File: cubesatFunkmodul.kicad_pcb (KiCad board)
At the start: 2 copper layers, 14 parts, among them IC1 74HC4050, U2 ATMEGA128-16AU, Y1 Crystal_GND23

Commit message: Cleares PCB
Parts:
- removed C1, C2, C3: C, Capacitors_SMD:C_0603
- removed C4, C5: 10pF, Capacitors_SMD:C_0603_HandSoldering
- removed C6: C, Capacitors_SMD:C_0603_HandSoldering
- removed D1: D, Diodes_SMD:D_0603
- removed IC1: 74HC4050, Housings_SSOP:SSOP-16_5.3x6.2mm_Pitch0.65mm
- removed L1: Ferrite_Bead, Inductors_SMD:L_0603_HandSoldering
- removed R1, R2, R3: R, Resistors_SMD:R_0603_HandSoldering
- removed U2: ATMEGA128-16AU, Housings_QFP:TQFP-64_14x14mm_Pitch0.8mm
- removed Y1: Crystal_GND23, Crystals:Crystal_SMD_0603-4pin_6.0x3.5mm_HandSoldering

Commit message: Adds new submodules
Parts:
- added C1: 10pF, Capacitors_SMD:C_0603_HandSoldering, F.Cu at (113.8, 115.8)
- added C2: 10pF, Capacitors_SMD:C_0603_HandSoldering, F.Cu at (121.6, 118.4)
- added C3: C, Capacitors_SMD:C_0603_HandSoldering, F.Cu at (140.7, 97.3)
- added C4: 100nF, Capacitors_SMD:C_0603, F.Cu at (136.9, 112.3)
- added C5: 100nF, Capacitors_SMD:C_0603, F.Cu at (157.0, 102.4)
- added C6: 100nF, Capacitors_SMD:C_0603, F.Cu at (153.2, 97.8)
- added D1: D, Diodes_SMD:D_0603, F.Cu at (155.3, 113.3)
- added IC1: 74HC4050, Housings_SSOP:SSOP-16_5.3x6.2mm_Pitch0.65mm, F.Cu at (102.5, 109.7)
- added L1: 10nH, Inductors_SMD:L_0603_HandSoldering, F.Cu at (157.6, 106.9)
- added R1: R, Resistors_SMD:R_0603_HandSoldering, F.Cu at (141.8, 104.6)
- added R2: R, Resistors_SMD:R_0603_HandSoldering, F.Cu at (147.2, 113.0)
- added R3: R, Resistors_SMD:R_0603_HandSoldering, F.Cu at (148.5, 103.1)
- added U1: ATMEGA128-16AU, Housings_QFP:TQFP-64_14x14mm_Pitch0.8mm, F.Cu at (123.2, 99.1)
- added Y1: Crystal_GND23, Crystals:Crystal_SMD_EuroQuartz_X22-4pin_2.5x2.0mm_HandSoldering, F.Cu at (130.7, 117.7)
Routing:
- net /Funkmodul1/+3.3V: track 0.00 -> 20.1 mm, vias 0 -> 1

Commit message: Adds Connectors
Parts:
- removed IC1: 74HC4050, Housings_SSOP:SSOP-16_5.3x6.2mm_Pitch0.65mm
- added C10: 100nF, Capacitors_SMD:C_0603_HandSoldering, F.Cu at (68.6, 101.1)
- added C11: 100nF, Capacitors_SMD:C_0603_HandSoldering, F.Cu at (88.7, 107.8)
- added C12: 100nF, Capacitors_SMD:C_0603_HandSoldering, F.Cu at (88.7, 100.1)
- added C13: 47µF, Capacitors_SMD:C_1210_HandSoldering, F.Cu at (235.5, 73.2)
- added C14: 47µF, Capacitors_SMD:C_1210_HandSoldering, F.Cu at (254.6, 99.6)
- added C15: 47µF, Capacitors_SMD:C_1210_HandSoldering, F.Cu at (255.3, 82.4)
- added C16: 47pF, Capacitors_SMD:C_1210_HandSoldering, F.Cu at (210.0, 76.9)
- added C17: 680pF, Capacitors_SMD:C_0603_HandSoldering, F.Cu at (225.4, 79.0)
- added C18: 12pF, Capacitors_SMD:C_0603_HandSoldering, F.Cu at (195.4, 94.8)
- added C19: 100nF, Capacitors_SMD:C_0603_HandSoldering, F.Cu at (196.0, 88.5)
- added C20: 100nF, Capacitors_SMD:C_0603_HandSoldering, F.Cu at (53.1, 159.4)
- added C7: 10pF, Capacitors_SMD:C_0603_HandSoldering, F.Cu at (64.9, 107.4)
- added C8: 10pF, Capacitors_SMD:C_0603_HandSoldering, F.Cu at (65.0, 100.0)
- added C9: 10nF, Capacitors_SMD:C_0603_HandSoldering, F.Cu at (67.8, 97.4)
- added D10: DZ2J036M0LCT-ND, Diodes_SMD:D_SOD-323F, F.Cu at (195.7, 103.4)
- added D11: SMF3.3, Diodes_SMD:D_SOD-123F, F.Cu at (217.6, 79.3)
- added D12: SMF3.3, Diodes_SMD:D_SOD-123F, F.Cu at (193.7, 82.3)
- added D13: SMF3.3, Diodes_SMD:D_SOD-123F, F.Cu at (205.9, 67.4)
- added D14: SMF3.3, Diodes_SMD:D_SOD-123F, F.Cu at (238.0, 111.7)
- added D15: SMF3.3, Diodes_SMD:D_SOD-123F, F.Cu at (256.2, 90.7)
- added D16: SMF3.3, Diodes_SMD:D_SOD-123F, F.Cu at (200.9, 61.6)
- added D17: SMF3.3, Diodes_SMD:D_SOD-123F, F.Cu at (189.7, 63.5)
- added D18: SMF3.3, Diodes_SMD:D_SOD-123F, F.Cu at (178.5, 63.7)
- added D2: STTH102A, Diodes_SMD:D_0603, F.Cu at (199.8, 70.0)
- added D3: STTH102A, Diodes_SMD:D_0603, F.Cu at (56.5, 165.9)
- added D4: STTH102A, Diodes_SMD:D_0603, F.Cu at (236.4, 93.3)
- added D5: STTH102A, Diodes_SMD:D_0603, F.Cu at (48.8, 158.4)
- added D6: STTH102A, Diodes_SMD:D_0603, F.Cu at (44.5, 169.7)
- added D7: STTH102A, Diodes_SMD:D_0603, F.Cu at (93.0, 101.4)
- added D8: STTH102A, Diodes_SMD:D_0603, F.Cu at (92.0, 106.7)
- added D9: STTH102A, Diodes_SMD:D_0603, F.Cu at (69.1, 94.4)
- added L2: 5µH, Inductors_SMD:L_6.3x6.3_H3, F.Cu at (235.7, 83.5)
- added Q1: MMBT5401-TP, TO_SOT_Packages_SMD:SOT-23, F.Cu at (207.5, 59.5)
- added Q2: AO3414, TO_SOT_Packages_SMD:SOT-23, F.Cu at (43.0, 94.3)
- added Q3: MMBT5551-TP, TO_SOT_Packages_SMD:SOT-23, F.Cu at (86.3, 86.7)
- added Q4: MMBT5551-TP, TO_SOT_Packages_SMD:SOT-23, F.Cu at (73.7, 86.3)
- added Q5: MMBT5551-TP, TO_SOT_Packages_SMD:SOT-23, F.Cu at (65.1, 86.2)
- added Q6: MMBT5551-TP, TO_SOT_Packages_SMD:SOT-23, F.Cu at (99.6, 86.6)
- added Q7: MMBT5551-TP, TO_SOT_Packages_SMD:SOT-23, F.Cu at (92.9, 86.6)
- added Q8: MMBT5551-TP, TO_SOT_Packages_SMD:SOT-23, F.Cu at (192.0, 49.0)
- added R10: 15k, Resistors_SMD:R_0603_HandSoldering, F.Cu at (156.9, 78.9)
- added R11: 100k, Resistors_SMD:R_0603_HandSoldering, F.Cu at (175.6, 104.2)
- added R12: 10k, Resistors_SMD:R_0603_HandSoldering, F.Cu at (92.7, 109.6)
- added R13: 10k, Resistors_SMD:R_0603_HandSoldering, F.Cu at (91.8, 103.7)
- added R14: 100k, Resistors_SMD:R_0603_HandSoldering, F.Cu at (70.6, 94.2)
- added R15: 100k, Resistors_SMD:R_0603_HandSoldering, F.Cu at (246.3, 52.4)
- added R16: 100k, Resistors_SMD:R_0603_HandSoldering, F.Cu at (188.8, 100.0)
- added R17: 100k, Resistors_SMD:R_0603_HandSoldering, F.Cu at (252.4, 53.9)
- added R18: 100R, Resistors_SMD:R_0603_HandSoldering, F.Cu at (181.4, 100.3)
- added R19: 10k, Resistors_SMD:R_0603_HandSoldering, F.Cu at (79.9, 85.9)
- added R20: 4k7, Resistors_SMD:R_0603_HandSoldering, F.Cu at (81.4, 85.9)
- added R21: 10k, Resistors_SMD:R_0603_HandSoldering, F.Cu at (99.8, 84.1)
- added R22: 10k, Resistors_SMD:R_0603_HandSoldering, F.Cu at (93.2, 84.1)
- added R23: 10k, Resistors_SMD:R_0603_HandSoldering, F.Cu at (86.5, 84.2)
- added R24: 10k, Resistors_SMD:R_0603_HandSoldering, F.Cu at (73.9, 83.8)
- added R25: 10k, Resistors_SMD:R_0603_HandSoldering, F.Cu at (65.3, 83.7)
- added R26: 4k7, Resistors_SMD:R_0603_HandSoldering, F.Cu at (97.0, 86.4)
- added R27: 4k7, Resistors_SMD:R_0603_HandSoldering, F.Cu at (90.4, 86.4)
- added R28: 4k7, Resistors_SMD:R_0603_HandSoldering, F.Cu at (83.8, 86.4)
- added R29: 4k7, Resistors_SMD:R_0603_HandSoldering, F.Cu at (71.1, 86.0)
- added R30: 4k7, Resistors_SMD:R_0603_HandSoldering, F.Cu at (62.6, 86.0)
- added R31: 10k, Resistors_SMD:R_0603_HandSoldering, F.Cu at (102.2, 86.9)
- added R32: 10k, Resistors_SMD:R_0603_HandSoldering, F.Cu at (95.5, 86.9)
- added R33: 10k, Resistors_SMD:R_0603_HandSoldering, F.Cu at (88.9, 86.9)
- added R34: 10k, Resistors_SMD:R_0603_HandSoldering, F.Cu at (76.2, 86.5)
- added R35: 10k, Resistors_SMD:R_0603_HandSoldering, F.Cu at (67.7, 86.5)
- added R36: 90k9, Resistors_SMD:R_0603_HandSoldering, F.Cu at (154.1, 105.2)
- added R37: 49k9, Resistors_SMD:R_0603_HandSoldering, F.Cu at (154.1, 110.1)
- added R38: 6k81, Resistors_SMD:R_0603_HandSoldering, F.Cu at (151.0, 81.2)
- added R39: 121k, Resistors_SMD:R_0603_HandSoldering, F.Cu at (147.5, 90.8)
- added R4: 47R, Resistors_SMD:R_0603_HandSoldering, F.Cu at (54.3, 156.3)
- added R40: 887k, Resistors_SMD:R_0603_HandSoldering, F.Cu at (146.6, 95.3)
- added R41: 10k, Resistors_SMD:R_0603_HandSoldering, F.Cu at (145.6, 101.2)
- added R42: 10k, Resistors_SMD:R_0603_HandSoldering, F.Cu at (225.0, 88.0)
- added R5: 100R, Resistors_SMD:R_0603_HandSoldering, F.Cu at (40.4, 94.3)
- added R6: 100k, Resistors_SMD:R_0603_HandSoldering, F.Cu at (56.9, 169.8)
- added R7: 100k, Resistors_SMD:R_0603_HandSoldering, F.Cu at (38.9, 94.3)
- added R8: 10k, Resistors_SMD:R_0603_HandSoldering, F.Cu at (226.9, 49.3)
- added R9: 100k, Resistors_SMD:R_0603_HandSoldering, F.Cu at (48.7, 160.0)
- added U3: ATMEGA128-16AU, Housings_QFP:TQFP-64_14x14mm_Pitch0.8mm, F.Cu at (78.6, 105.1)
- added U4: LTC3113, Housings_SSOP:HTSSOP-20-1EP_4.4x6.5mm_Pitch0.65mm_ThermalPad, F.Cu at (247.0, 72.7)
- C1: value 10pF -> 10µF; footprint Capacitors_SMD:C_0603_HandSoldering -> Capacitors_SMD:C_1210_HandSoldering
- C2: value 10pF -> 1µF; footprint Capacitors_SMD:C_0603_HandSoldering -> Capacitors_SMD:C_1210_HandSoldering
- C3: value C -> 1nF
- C4: value 100nF -> 10µF; footprint Capacitors_SMD:C_0603 -> Capacitors_SMD:C_1210_HandSoldering
- C5, C6: footprint Capacitors_SMD:C_0603 -> Capacitors_SMD:C_0603_HandSoldering
- D1: value D -> STTH102A
- R1: value R -> 22k
- R2, R3: value R -> 100k
- U1: value ATMEGA128-16AU -> MC74HC4538A; footprint Housings_QFP:TQFP-64_14x14mm_Pitch0.8mm -> Housings_SOIC:SOIC-16_3.9x9.9mm_Pitch1.27mm
- Y1: value Crystal_GND23 -> Crystal_GND24; footprint Crystals:Crystal_SMD_EuroQuartz_X22-4pin_2.5x2.0mm_HandSoldering -> Crystals:Crystal_SMD_3225-4pin_3.2x2.5mm_HandSoldering
- moved R3 110.1 mm to (57.0, 164.3), turned to 180 degrees
- moved C3 109.2 mm to (56.9, 167.4), turned to 180 degrees
- moved C4 106.8 mm to (42.9, 163.1), turned to 90 degrees
- moved U1 99.3 mm to (50.4, 166.6)
- moved C5 91.6 mm to (247.7, 90.0)
- moved C2 89.8 mm to (203.3, 80.9)
- moved C1 72.4 mm to (57.9, 161.8), turned to 180 degrees
- moved R2 70.0 mm to (187.7, 56.0)
- moved Y1 67.3 mm to (64.9, 103.7), turned to 90 degrees
- moved L1 67.2 mm to (90.7, 100.2), turned to 270 degrees
- moved C6 61.8 mm to (91.8, 105.2), turned to 180 degrees
- moved R1 61.0 mm to (176.3, 54.4)
- moved D1 55.7 mm to (193.7, 73.0)
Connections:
- C1 pad 2: /Funkmodul1/GND -> GND
- C2 pad 1: /Funkmodul1/GND -> GND
- C2 pad 2: Net-(C2-Pad2) -> /Connector/3.3V
- C3 pad 1: ATMEGA-RESET -> /Connector/3.3V
- C3 pad 2: /Funkmodul1/GND -> Net-(C3-Pad2)
- C4 pad 1: /Funkmodul1/GND -> Net-(C4-Pad1)
- C4 pad 2: /Funkmodul1/+3.3V -> GND
- C5 pad 1: /Funkmodul1/GND -> GND
- C5 pad 2: /Funkmodul1/+3.3V -> /Funkmodul1/VCC
- C6 pad 1: /Funkmodul1/GND -> Net-(C6-Pad1)
- C6 pad 2: Net-(C6-Pad2) -> GND
- D1 pad 1: /Funkmodul1/+3.3V -> Net-(D1-Pad1)
- D1 pad 2: ATMEGA-RESET -> /Connector/~ENABLE1~
- L1 pad 1: Net-(C6-Pad2) -> Net-(C12-Pad2)
- L1 pad 2: /Funkmodul1/+3.3V -> /Funkmodul1/VCC
- R1 pad 1: /Funkmodul1/+3.3V -> Net-(D1-Pad1)
- R1 pad 2: ATMEGA-RESET -> GND
- R2 pad 1: /Funkmodul1/Funkeinheit/MISO -> /Funkmodul1/~ON~
- R2 pad 2: /Funkmodul1/GND -> GND
- R3 pad 1: /Funkmodul1/Funkeinheit/MISO -> Net-(D3-Pad1)
- R3 pad 2: /Funkmodul1/Funkeinheit/MISO -> Net-(C1-Pad1)
- U1 pad 1: Net-(U1-Pad1) -> GND
- U1 pad 10: /Funkmodul1/Funkeinheit/SS -> Net-(R6-Pad1)
- U1 pad 11: /Funkmodul1/Funkeinheit/SCK -> Net-(U1-Pad11)
- U1 pad 12: /Funkmodul1/Funkeinheit/MOSI -> Net-(C3-Pad2)
- U1 pad 13: /Funkmodul1/Funkeinheit/MISO -> /Connector/3.3V
- U1 pad 14: Net-(U1-Pad14) -> Net-(C1-Pad1)
- U1 pad 15: Net-(U1-Pad15) -> GND
- U1 pad 2: /Funkmodul1/RX -> Net-(C4-Pad1)
- U1 pad 3: /Funkmodul1/TX -> /Connector/3.3V
- U1 pad 4: Net-(U1-Pad4) -> /Funkmodul1/WDG_TRIGGER
- U1 pad 5: Net-(U1-Pad5) -> Net-(R6-Pad1)
- U1 pad 6: Net-(U1-Pad6) -> Net-(U1-Pad11)
- U1 pad 8: Net-(U1-Pad8) -> GND
- U1 pad 9: Net-(U1-Pad9) -> (no net)
- Y1 pad 1: Net-(C1-Pad1) -> Net-(C7-Pad1)
- Y1 pad 2: /Funkmodul1/GND -> GND
- Y1 pad 3: /Funkmodul1/GND -> Net-(C8-Pad2)
- Y1 pad 4: Net-(C2-Pad2) -> GND
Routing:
- net /Funkmodul1/Funkeinheit/SCK: track 0.00 -> 34.8 mm
- net /Funkmodul1/Funkeinheit/SS: track 0.00 -> 33.2 mm
- net Net-(D3-Pad1): track 0.00 -> 32.3 mm
- net /Funkmodul1/Funkeinheit/MOSI: track 0.00 -> 30.7 mm
- net /Funkmodul1/Funkeinheit/MISO: track 0.00 -> 30.1 mm
- net GND: track 0.00 -> 29.7 mm, vias 0 -> 20
- net /Funkmodul1/VCC: track 0.00 -> 28.5 mm, vias 0 -> 10
- net /Funkmodul1/+3.3V: track 20.1 -> 0.00 mm, vias 1 -> 0
- net /Funkmodul1/Funkeinheit/TXON: track 0.00 -> 18.6 mm
- net Net-(R6-Pad1): track 0.00 -> 18.0 mm
- net Net-(C20-Pad1): track 0.00 -> 14.6 mm
- net /Funkmodul1/Funkeinheit/RXON: track 0.00 -> 14.6 mm
- net Net-(C4-Pad1): track 0.00 -> 12.3 mm
- net Net-(C1-Pad1): track 0.00 -> 10.9 mm, vias 0 -> 1
- net Net-(C8-Pad2): track 0.00 -> 10.3 mm
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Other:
- board outline added: 85 x 85 mm
- net class Default: clearance 0.2 -> 0.2032; trace_width 0.25 -> 0.2032; via_drill 0.4 -> 0.3
- net class Supply added: clearance 0.2032, trace_width 0.508, via_dia 0.6, via_drill 0.3
- rule trace_clearance: 0.2 -> 0.2032

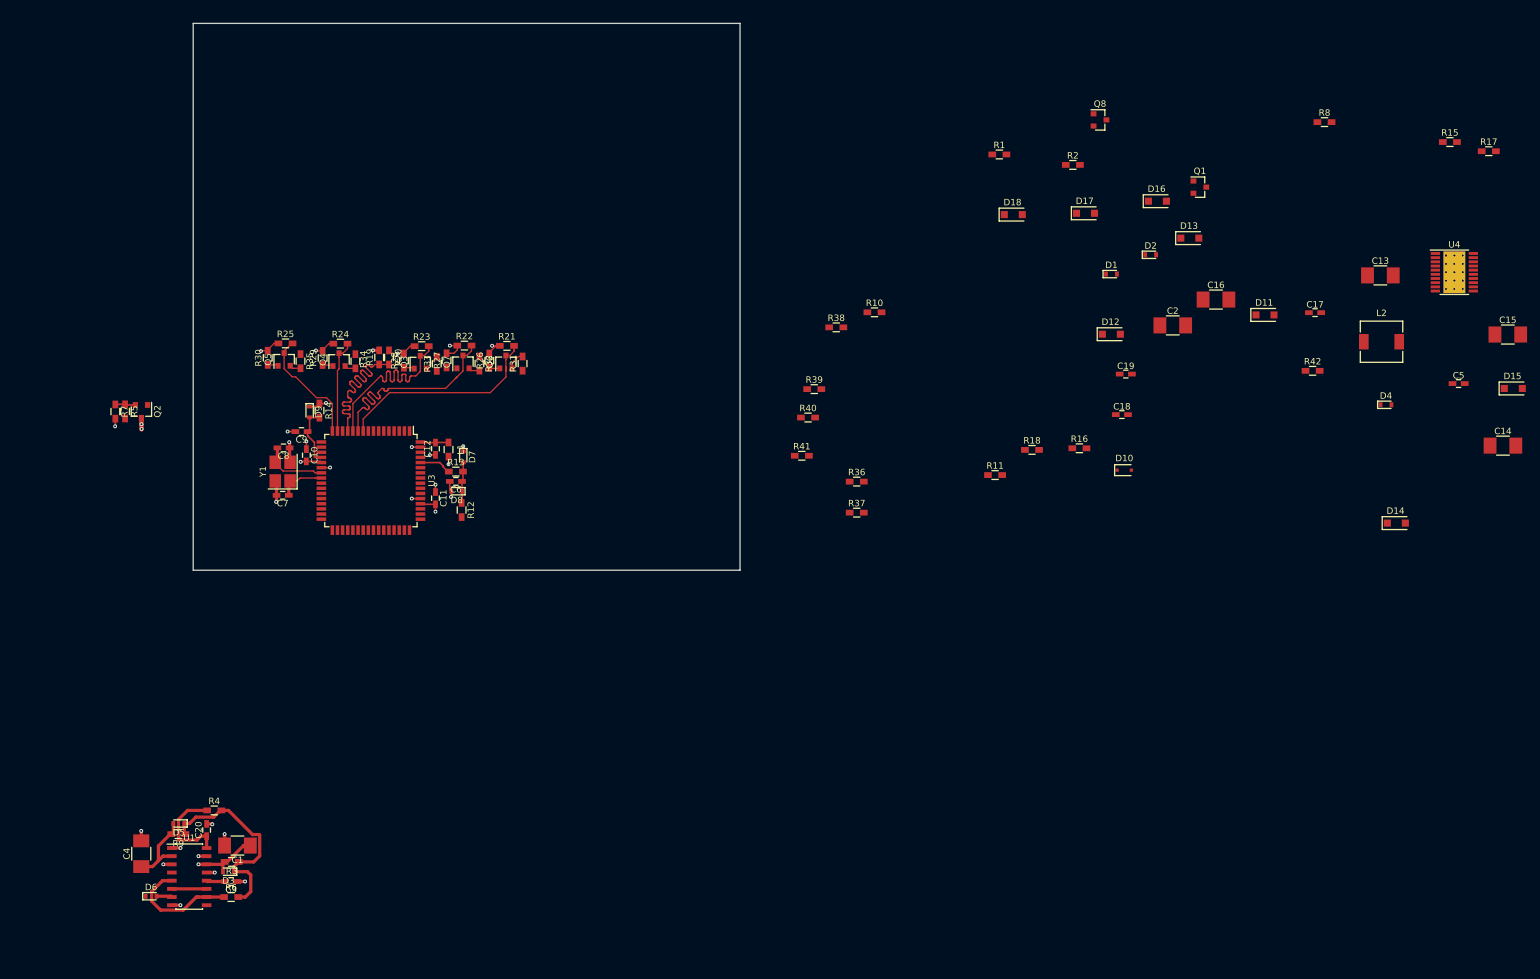
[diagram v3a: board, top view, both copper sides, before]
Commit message: Adds RFM23BP Footprint and places module on board
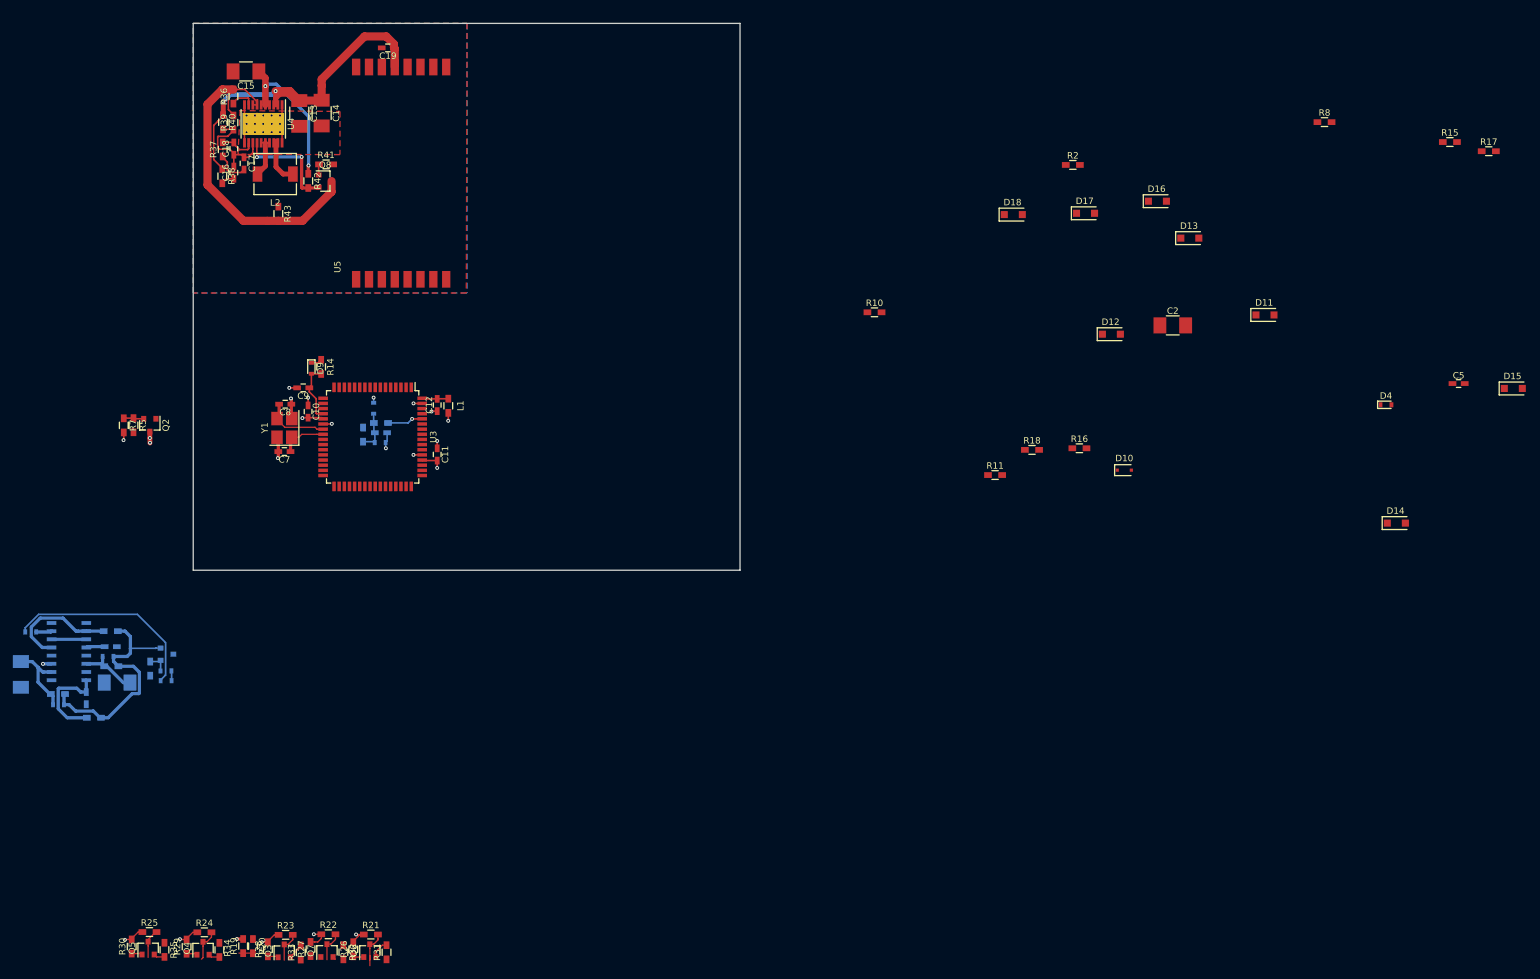
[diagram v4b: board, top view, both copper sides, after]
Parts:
- added R43: 0R, Resistors_SMD:R_0603_HandSoldering, F.Cu at (64.2, 63.6)
- added U5: RFM23BP, HopeRF:RFM23BP, F.Cu at (82.9, 60.5)
- C1, C20, C3, C4, C6, D1, D2, D3, D5, D6, D7, D8, Q1, R1, R12, R13, R3, R4, R6, R9, U1: moved to B.Cu
- C16: footprint Capacitors_SMD:C_1210_HandSoldering -> Capacitors_SMD:C_0603_HandSoldering
- moved C15 200.4 mm to (59.2, 41.5), turned to 180 degrees
- moved C14 190.8 mm to (71.0, 47.9), turned to 270 degrees
- moved U4 186.6 mm to (61.9, 49.6), turned to 270 degrees
- moved Q1 176.2 mm to (46.9, 132.1)
- moved L2 173.9 mm to (63.7, 57.4), turned to 180 degrees
- moved C13 169.9 mm to (67.5, 48.0), turned to 270 degrees
- moved C17 168.1 mm to (58.9, 55.8), turned to 270 degrees
- moved D2 166.7 mm to (46.8, 136.2)
- moved D1 159.4 mm to (46.8, 134.7)
- moved R42 158.9 mm to (68.9, 58.5), turned to 270 degrees
- moved R1 154.3 mm to (44.3, 134.3), turned to 270 degrees
- moved C16 153.9 mm to (57.3, 57.2), turned to 90 degrees
- moved C18 144.1 mm to (57.3, 53.5), turned to 90 degrees
- moved C19 125.4 mm to (81.3, 37.8), turned to 180 degrees
- moved Q8 120.8 mm to (71.5, 58.5)
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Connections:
- C13 pad 2: GND -> /Funkmodul1/Funkeinheit/PGND
- C14 pad 2: GND -> /Funkmodul1/Funkeinheit/PGND
- C15 pad 2: GND -> /Funkmodul1/Funkeinheit/PGND
- C19 pad 2: GND -> /Funkmodul1/Funkeinheit/PGND
- R20 pad 1: (no net) -> /Funkmodul1/Funkeinheit/MISO_
- U3 pad 25: (no net) -> /Funkmodul1/Funkeinheit/NIRQ
- U4 pad 1: GND -> /Funkmodul1/Funkeinheit/PGND
- U4 pad 10: GND -> /Funkmodul1/Funkeinheit/PGND
- U4 pad 11: GND -> /Funkmodul1/Funkeinheit/PGND
- U4 pad 20: GND -> /Funkmodul1/Funkeinheit/PGND
- U4 pad 21: GND -> /Funkmodul1/Funkeinheit/PGND
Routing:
- net /Funkmodul1/Funkeinheit/5V: track 0.00 -> 56.9 mm, vias 0 -> 2
- net GND: track 29.7 -> 75.3 mm, vias 20 -> 14
- net /Funkmodul1/~ON~: track 0.00 -> 31.4 mm
- net /Funkmodul1/Funkeinheit/SCK: track 34.8 -> 4.84 mm
- net /Funkmodul1/Funkeinheit/MISO: track 30.1 -> 2.44 mm
- net /Funkmodul1/Funkeinheit/SS: track 33.2 -> 6.39 mm
- net /Funkmodul1/Funkeinheit/MOSI: track 30.7 -> 4.83 mm
- net VBAT: track 0.00 -> 25.2 mm, vias 0 -> 2
- net Net-(Q8-Pad2): track 0.00 -> 16.7 mm, vias 0 -> 2
- net Net-(C16-Pad2): track 0.00 -> 16.6 mm
- net /Funkmodul1/Funkeinheit/PGND: track 0.00 -> 15.6 mm
- net /Funkmodul1/Funkeinheit/TXON: track 18.6 -> 4.56 mm
- net /Funkmodul1/Funkeinheit/RXON: track 14.6 -> 5.17 mm
- net Net-(L2-Pad1): track 0.00 -> 8.19 mm
- net Net-(L2-Pad2): track 0.00 -> 7.30 mm
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- added copper zone on B.Cu, net /Funkmodul1/Funkeinheit/PGND
- added copper zone on F.Cu, net /Funkmodul1/Funkeinheit/PGND
- added copper zone on In1.Cu, net /Funkmodul1/Funkeinheit/PGND
- added copper zone on F.Cu, net GND
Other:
- copper layers 2 -> 4
